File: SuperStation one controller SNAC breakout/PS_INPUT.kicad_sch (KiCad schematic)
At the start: 4 parts, among them J3 Conn_01x09_Pin, J6 Conn_01x09_Pin

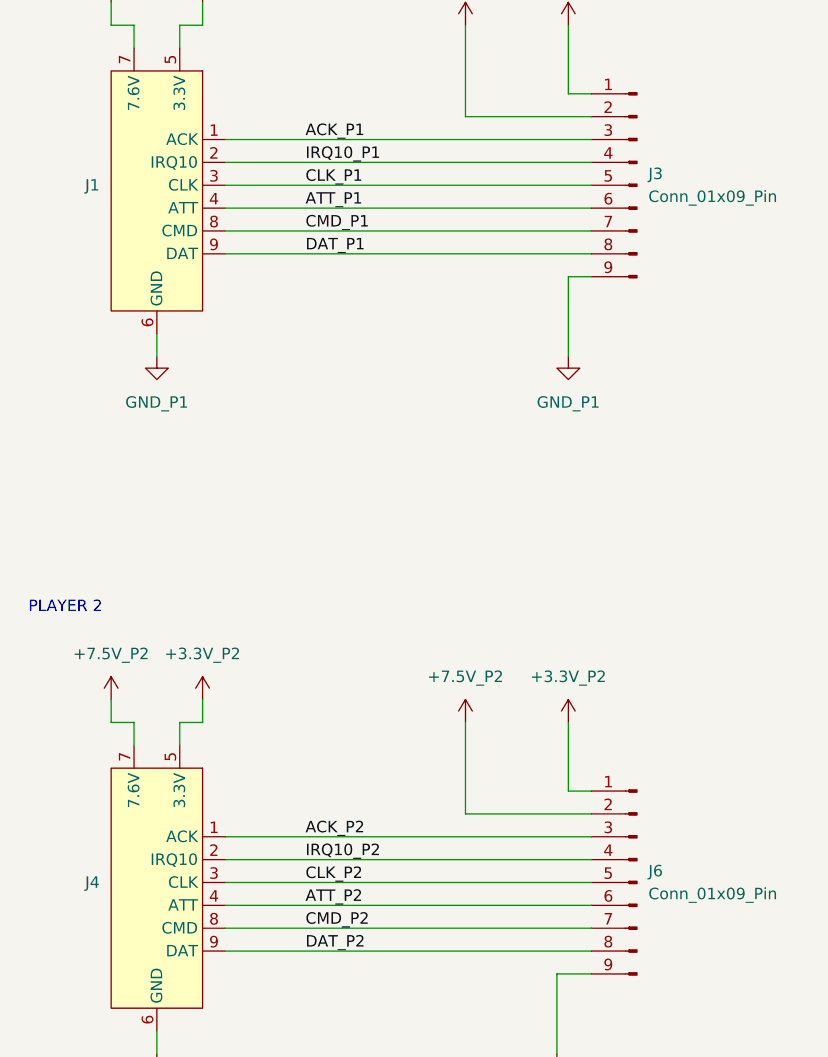
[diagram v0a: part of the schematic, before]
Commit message: added power sheet to schematic and started rough pcb placement
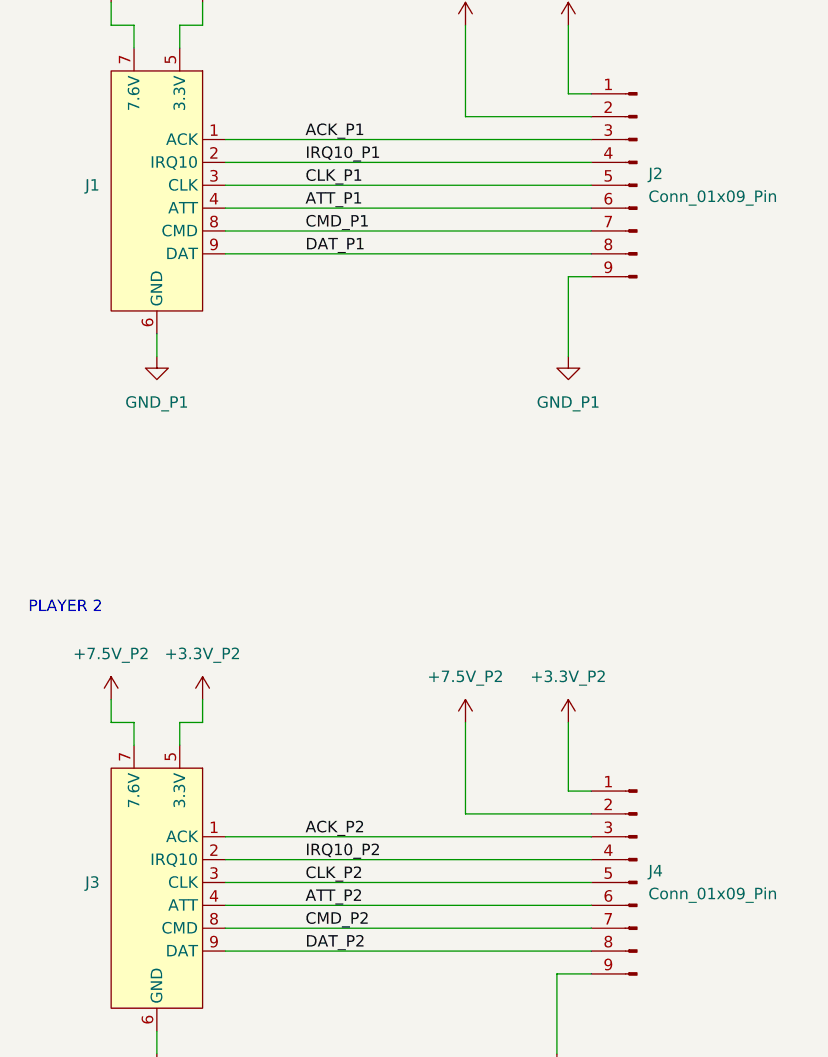
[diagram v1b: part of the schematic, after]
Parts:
- J1: footprint (none) -> Connector_PinHeader_2.54mm:PinHeader_1x09_P2.54mm_Vertical
- J2: renamed from J3; footprint (none) -> Connector_JST:JST_PH_S8B-PH-SM4-TB_1x08-1MP_P2.00mm_Horizontal
- J3: renamed from J4; footprint (none) -> Connector_PinHeader_2.54mm:PinHeader_1x09_P2.54mm_Vertical
- J4: renamed from J6; footprint (none) -> Connector_JST:JST_PH_S8B-PH-SM4-TB_1x08-1MP_P2.00mm_Horizontal
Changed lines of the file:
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@@
 		(dnp no)
 		(fields_autoplaced yes)
-		(property "Reference" "#PWR01"
+		(property "Reference" "#PWR07"
 			(at 113.03 173.99 0)
 			(effects
@@
 			(project "SuperStation one controller SNAC breakout"
 				(path "/cbd92933-d20e-42b7-906c-813e5f34c94a/f156f76a-3de3-4cde-8fa6-723ea9336b7e"
-					(reference "#PWR01")
+					(reference "#PWR07")
 					(unit 1)
 				)
@@
 		(dnp no)
 		(fields_autoplaced yes)
-		(property "Reference" "#PWR035"
+		(property "Reference" "#PWR04"
 			(at 163.83 99.06 0)
 			(effects
@@
 			(project "SuperStation one controller SNAC breakout"
 				(path "/cbd92933-d20e-42b7-906c-813e5f34c94a/f156f76a-3de3-4cde-8fa6-723ea9336b7e"
-					(reference "#PWR035")
+					(reference "#PWR04")
 					(unit 1)
 				)
@@
 		(dnp no)
 		(fields_autoplaced yes)
-		(property "Reference" "J6"
+		(property "Reference" "J4"
 			(at 172.72 189.2299 0)
 			(effects
@@
 			)
 		)
-		(property "Footprint" ""
+		(property "Footprint" "Connector_JST:JST_PH_S8B-PH-SM4-TB_1x08-1MP_P2.00mm_Horizontal"
 			(at 171.45 190.5 0)
 			(effects
@@
 			(project "SuperStation one controller SNAC breakout"
 				(path "/cbd92933-d20e-42b7-906c-813e5f34c94a/f156f76a-3de3-4cde-8fa6-723ea9336b7e"
-					(reference "J6")
+					(reference "J4")
 					(unit 1)
 				)
@@
 		(dnp no)
 		(fields_autoplaced yes)
-		(property "Reference" "#PWR026"
+		(property "Reference" "#PWR012"
 			(at 162.56 215.9 0)
 			(effects
@@
 			(project "SuperStation one controller SNAC breakout"
 				(path "/cbd92933-d20e-42b7-906c-813e5f34c94a/f156f76a-3de3-4cde-8fa6-723ea9336b7e"
-					(reference "#PWR026")
+					(reference "#PWR012")
 					(unit 1)
 				)
@@
 		(dnp no)
 		(fields_autoplaced yes)
-		(property "Reference" "#PWR032"
+		(property "Reference" "#PWR02"
 			(at 123.19 96.52 0)
 			(effects
@@
 			(project "SuperStation one controller SNAC breakout"
 				(path "/cbd92933-d20e-42b7-906c-813e5f34c94a/f156f76a-3de3-4cde-8fa6-723ea9336b7e"
-					(reference "#PWR032")
+					(reference "#PWR02")
 					(unit 1)
 				)
@@
 		(dnp no)
 		(fields_autoplaced yes)
-		(property "Reference" "#PWR03"
+		(property "Reference" "#PWR08"
 			(at 123.19 173.99 0)
 			(effects
@@
 			(project "SuperStation one controller SNAC breakout"
 				(path "/cbd92933-d20e-42b7-906c-813e5f34c94a/f156f76a-3de3-4cde-8fa6-723ea9336b7e"
-					(reference "#PWR03")
+					(reference "#PWR08")
 					(unit 1)
 				)
@@
 		(dnp no)
 		(fields_autoplaced yes)
-		(property "Reference" "#PWR036"
+		(property "Reference" "#PWR06"
 			(at 163.83 138.43 0)
 			(effects
@@
 			(project "SuperStation one controller SNAC breakout"
 				(path "/cbd92933-d20e-42b7-906c-813e5f34c94a/f156f76a-3de3-4cde-8fa6-723ea9336b7e"
-					(reference "#PWR036")
+					(reference "#PWR06")
 					(unit 1)
 				)
@@
 		(dnp no)
 		(fields_autoplaced yes)
-		(property "Reference" "#PWR028"
+		(property "Reference" "#PWR01"
 			(at 113.03 96.52 0)
 			(effects
@@
 			(project "SuperStation one controller SNAC breakout"
 				(path "/cbd92933-d20e-42b7-906c-813e5f34c94a/f156f76a-3de3-4cde-8fa6-723ea9336b7e"
-					(reference "#PWR028")
+					(reference "#PWR01")
 					(unit 1)
 				)
@@
 		(dnp no)
 		(fields_autoplaced yes)
-		(property "Reference" "#PWR025"
+		(property "Reference" "#PWR010"
 			(at 163.83 176.53 0)
 			(effects
@@
 			(project "SuperStation one controller SNAC breakout"
 				(path "/cbd92933-d20e-42b7-906c-813e5f34c94a/f156f76a-3de3-4cde-8fa6-723ea9336b7e"
-					(reference "#PWR025")
+					(reference "#PWR010")
 					(unit 1)
 				)
@@
 		(dnp no)
 		(fields_autoplaced yes)
-		(property "Reference" "J3"
+		(property "Reference" "J2"
 			(at 172.72 111.7599 0)
 			(effects
@@
 			)
 		)
-		(property "Footprint" ""
+		(property "Footprint" "Connector_JST:JST_PH_S8B-PH-SM4-TB_1x08-1MP_P2.00mm_Horizontal"
 			(at 171.45 113.03 0)
 			(effects
@@
 			(project ""
 				(path "/cbd92933-d20e-42b7-906c-813e5f34c94a/f156f76a-3de3-4cde-8fa6-723ea9336b7e"
-					(reference "J3")
+					(reference "J2")
 					(unit 1)
 				)
@@
 		(dnp no)
 		(fields_autoplaced yes)
-		(property "Reference" "#PWR034"
+		(property "Reference" "#PWR03"
 			(at 152.4 99.06 0)
 			(effects
@@
 			(project "SuperStation one controller SNAC breakout"
 				(path "/cbd92933-d20e-42b7-906c-813e5f34c94a/f156f76a-3de3-4cde-8fa6-723ea9336b7e"
-					(reference "#PWR034")
+					(reference "#PWR03")
 					(unit 1)
 				)
@@
 		(dnp no)
 		(fields_autoplaced yes)
-		(property "Reference" "#PWR024"
+		(property "Reference" "#PWR09"
 			(at 152.4 176.53 0)
 			(effects
@@
 			(project "SuperStation one controller SNAC breakout"
 				(path "/cbd92933-d20e-42b7-906c-813e5f34c94a/f156f76a-3de3-4cde-8fa6-723ea9336b7e"
-					(reference "#PWR024")
+					(reference "#PWR09")
 					(unit 1)
 				)
@@
 		(dnp no)
 		(fields_autoplaced yes)
-		(property "Reference" "J4"
+		(property "Reference" "J3"
 			(at 111.76 190.4999 0)
 			(effects
@@
 			)
 		)
-		(property "Footprint" ""
+		(property "Footprint" "Connector_PinHeader_2.54mm:PinHeader_1x09_P2.54mm_Vertical"
 			(at 123.19 177.8 0)
 			(effects
@@
 			(project "SuperStation one controller SNAC breakout"
 				(path "/cbd92933-d20e-42b7-906c-813e5f34c94a/f156f76a-3de3-4cde-8fa6-723ea9336b7e"
-					(reference "J4")
+					(reference "J3")
 					(unit 1)
 				)
@@
 		(dnp no)
 		(fields_autoplaced yes)
-		(property "Reference" "#PWR033"
+		(property "Reference" "#PWR011"
 			(at 118.11 215.9 0)
 			(effects
@@
 			(project "SuperStation one controller SNAC breakout"
 				(path "/cbd92933-d20e-42b7-906c-813e5f34c94a/f156f76a-3de3-4cde-8fa6-723ea9336b7e"
-					(reference "#PWR033")
+					(reference "#PWR011")
 					(unit 1)
 				)
@@
 			)
 		)
-		(property "Footprint" ""
+		(property "Footprint" "Connector_PinHeader_2.54mm:PinHeader_1x09_P2.54mm_Vertical"
 			(at 123.19 100.33 0)
 			(effects
@@
 		(dnp no)
 		(fields_autoplaced yes)
-		(property "Reference" "#PWR023"
+		(property "Reference" "#PWR05"
 			(at 118.11 138.43 0)
 			(effects
@@
 			(project "SuperStation one controller SNAC breakout"
 				(path "/cbd92933-d20e-42b7-906c-813e5f34c94a/f156f76a-3de3-4cde-8fa6-723ea9336b7e"
-					(reference "#PWR023")
-					(unit 1)
-				)
+					(reference "#PWR05")
+					(unit 1)
+				)

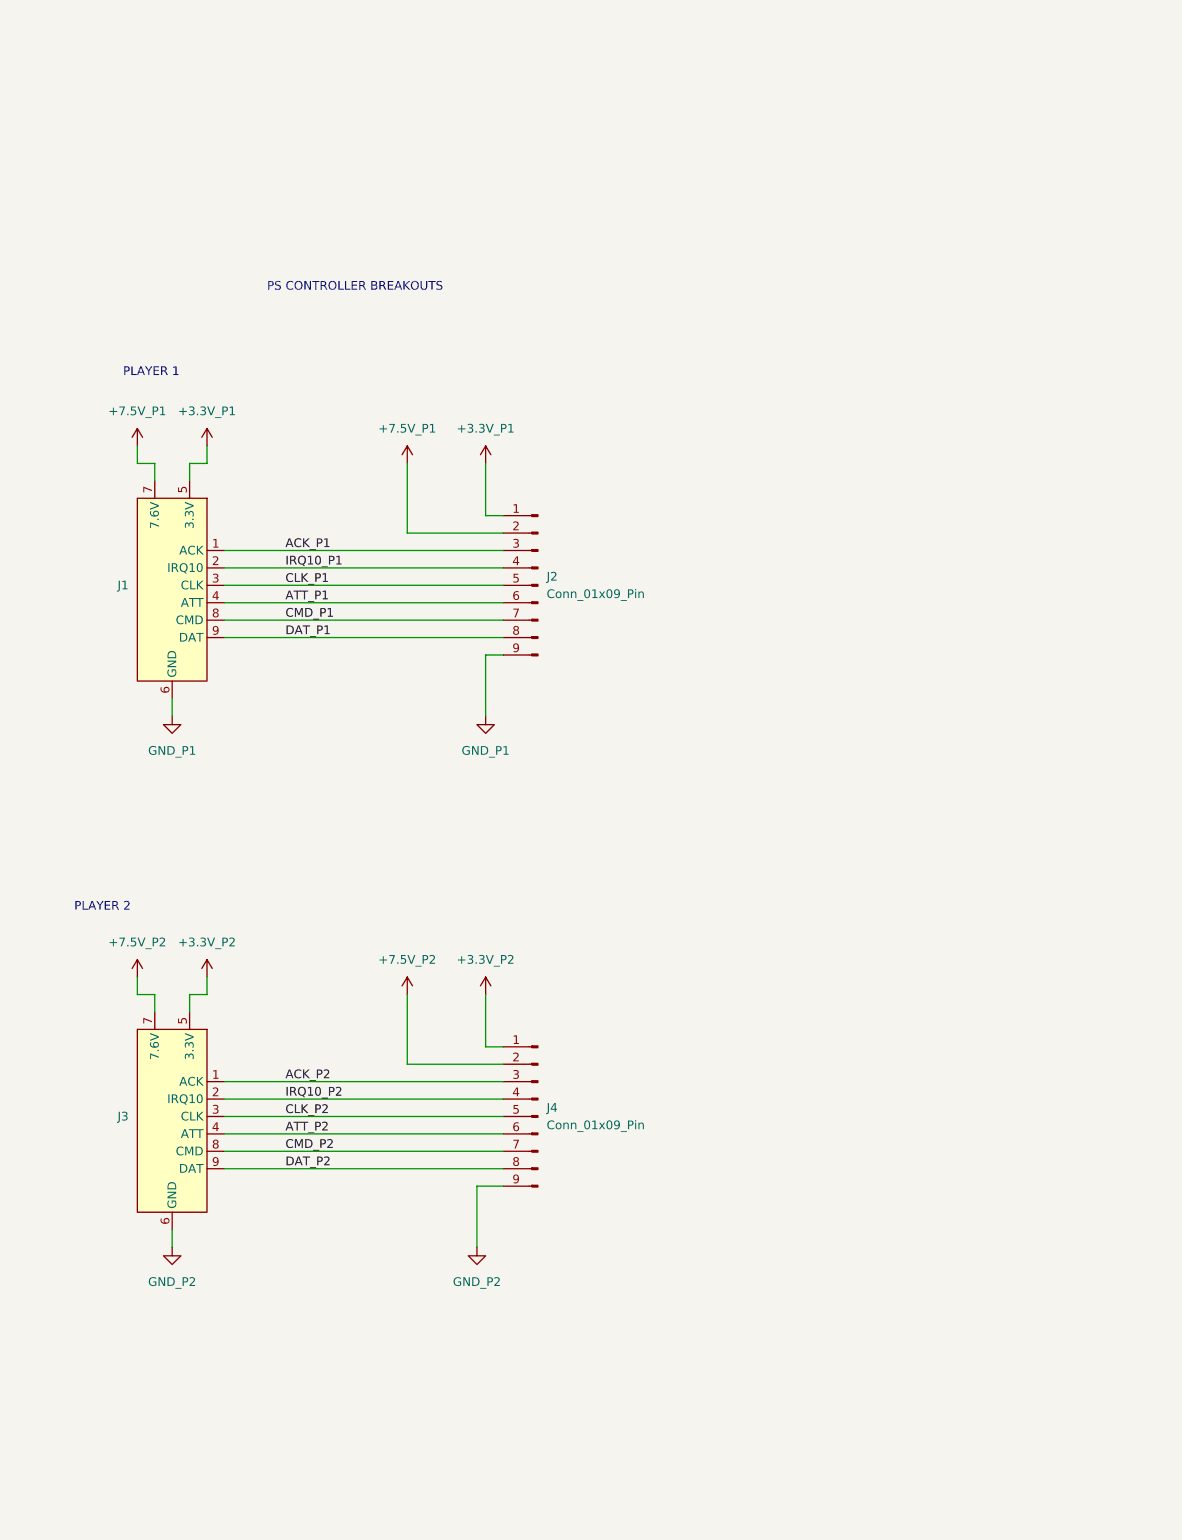
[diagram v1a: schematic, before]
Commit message: board layout and added debug breakouts for all signals
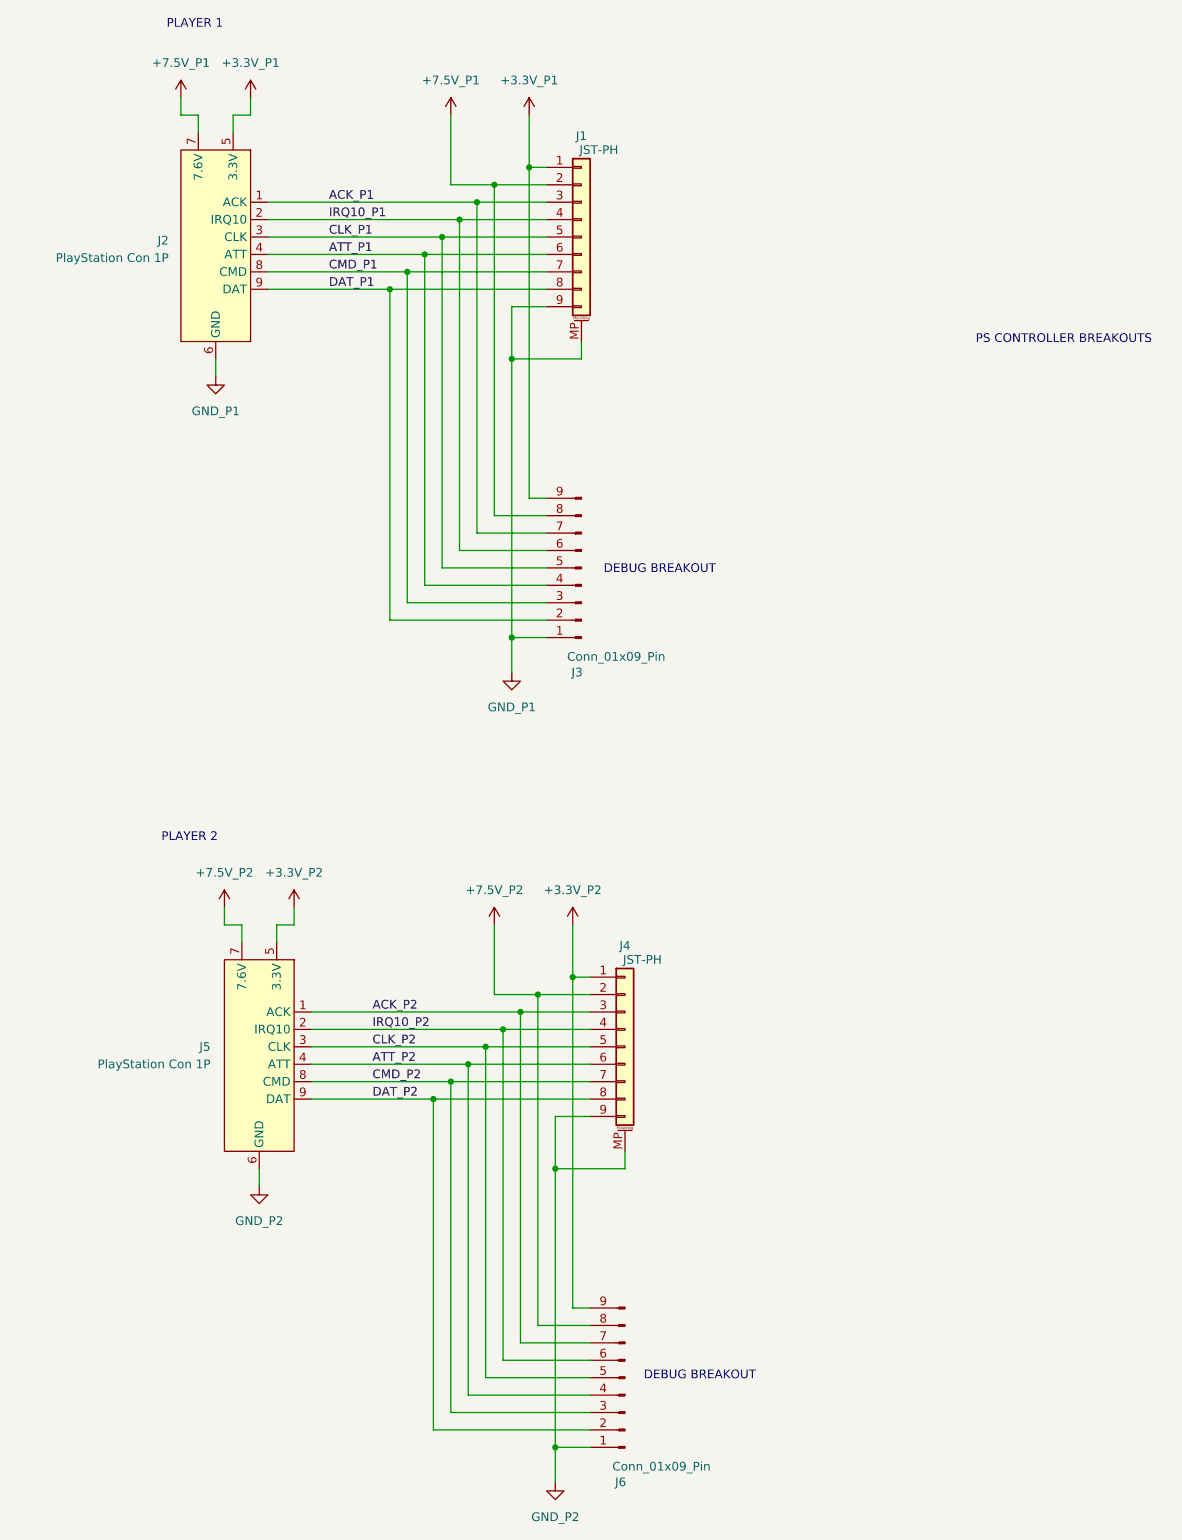
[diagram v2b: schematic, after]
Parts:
- removed J1, J3: ~, Connector_PinHeader_2.54mm:PinHeader_1x09_P2.54mm_Vertical, symbol Nick_Connector:PS2_Controller_1P
- added J2, J5: PlayStation Con 1P, Nick_Connectors:PlayStation 1P, symbol Nick_Connector:PlayStation Controller 1P
- added J3, J6: Conn_01x09_Pin, Connector_PinHeader_2.54mm:PinHeader_1x09_P2.54mm_Vertical, symbol Connector:Conn_01x09_Pin
- J1: renamed from J2; value Conn_01x09_Pin -> JST-PH; footprint Connector_JST:JST_PH_S8B-PH-SM4-TB_1x08-1MP_P2.00mm_Horizontal -> Connector_JST:JST_PH_S9B-PH-SM4-TB_1x09-1MP_P2.00mm_Horizontal; symbol Connector:Conn_01x09_Pin -> Connector_Generic_MountingPin:Conn_01x09_MountingPin
- J4: value Conn_01x09_Pin -> JST-PH; footprint Connector_JST:JST_PH_S8B-PH-SM4-TB_1x08-1MP_P2.00mm_Horizontal -> Connector_JST:JST_PH_S9B-PH-SM4-TB_1x09-1MP_P2.00mm_Horizontal; symbol Connector:Conn_01x09_Pin -> Connector_Generic_MountingPin:Conn_01x09_MountingPin
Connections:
- net +3.3V_P1: now also J2.5 (3.3V), J3.9 (Pin_9)
- net +3.3V_P2: now also J5.5 (3.3V), J6.9 (Pin_9)
- net +7.5V_P1: now also J2.7 (7.6V), J3.8 (Pin_8)
- net +7.5V_P2: now also J5.7 (7.6V), J6.8 (Pin_8)
- net ACK_P1: now also J2.1 (ACK), J3.7 (Pin_7)
- net ACK_P2: now also J5.1 (ACK), J6.7 (Pin_7)
- net ATT_P1: now also J2.4 (ATT), J3.4 (Pin_4)
- net ATT_P2: now also J5.4 (ATT), J6.4 (Pin_4)
- net CLK_P1: now also J2.3 (CLK), J3.5 (Pin_5)
- net CLK_P2: now also J5.3 (CLK), J6.5 (Pin_5)
- net CMD_P1: now also J2.8 (CMD), J3.3 (Pin_3)
- net CMD_P2: now also J5.8 (CMD), J6.3 (Pin_3)
- net DAT_P1: now also J2.9 (DAT), J3.2 (Pin_2)
- net DAT_P2: now also J5.9 (DAT), J6.2 (Pin_2)
- net GND_P1: now also J1.MP (MountPin), J2.6 (GND), J3.1 (Pin_1)
- net GND_P2: now also J4.MP (MountPin), J5.6 (GND), J6.1 (Pin_1)
- net IRQ10_P1: now also J2.2 (IRQ10), J3.6 (Pin_6)
- net IRQ10_P2: now also J5.2 (IRQ10), J6.6 (Pin_6)
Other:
- note added: "DEBUG BREAKOUT"
